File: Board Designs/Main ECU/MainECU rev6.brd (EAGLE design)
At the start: 120.6 x 78.9 mm, 191 parts, among them J1 JUMPER, J2 JUMPER, J3 JUMPER, J4 JUMPER, J5 JUMPER, J6 JUMPER, Q1 P-CHANNEL_MOSFET_DMP3099L-7, Q12 P-CHANNEL_MOSFET_DMP3099L-7, X1 CONNECTOR-37, X2 CONNECTOR-4AUTOSPORT, X3 CONNECTOR-4NANO-FIT-VERTICAL-4, X4 CONNECTOR-4NANO-FIT-VERTICAL-4

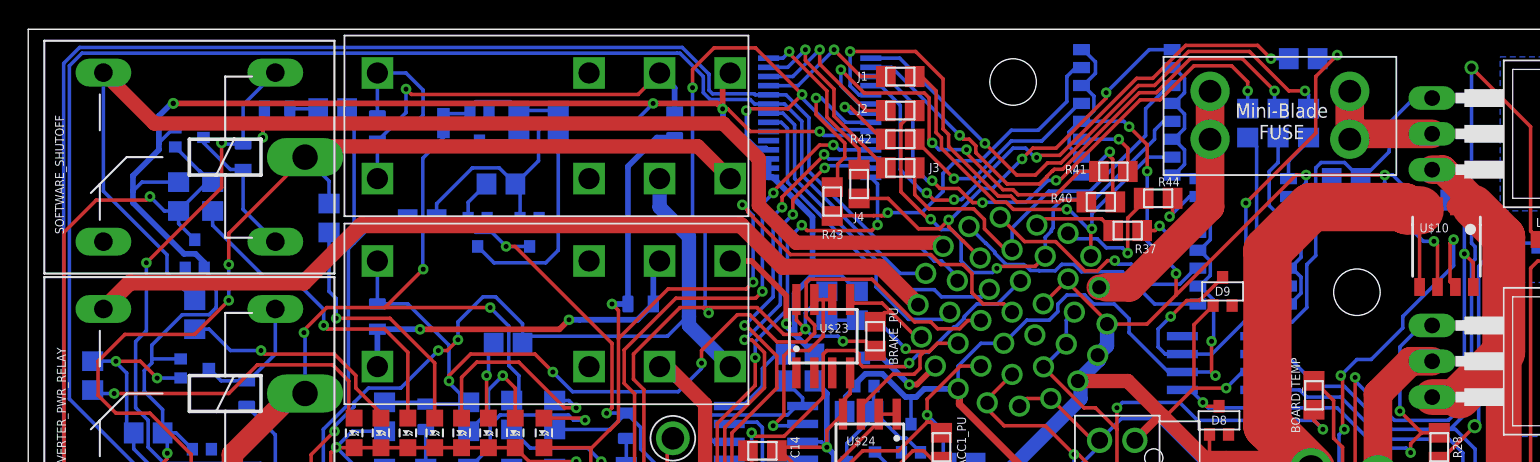
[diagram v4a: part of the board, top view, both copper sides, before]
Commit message: Main ECU rev6: Add optional diode to drop IMD relay coil voltage
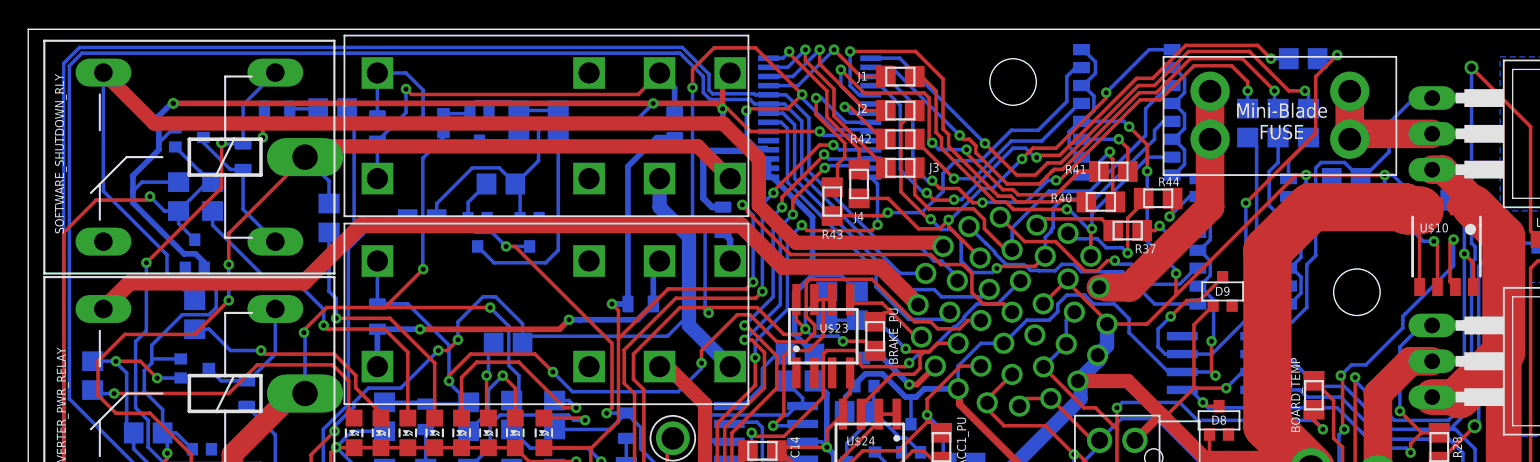
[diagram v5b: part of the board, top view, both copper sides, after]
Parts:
- added D23: TS4148 RYG, HyTechDevices:0805_D
- BMS_SHUTDOWN_RLY: value RT424009 -> RT424012
- renumbered IMD_SHUTDOWN to IMD_SHUTDOWN_RLY, IMD_SHUTDOWN1 to BMS_SHUTDOWN_RLY, SOFTWARE_SHUTOFF to SOFTWARE_SHUTDOWN_RLY
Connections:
- new net N$60: D23.A, IMD_SHUTDOWN_RLY.4
- net GND: now also D23.C; no longer IMD_SHUTDOWN_RLY.4
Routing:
- net N$60: track 0.00 -> 2.23 mm
- net GND: vias 36 -> 35
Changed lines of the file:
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@@
 <attribute name="VALUE" x="24.0538" y="58.547" size="0.3048" layer="28" font="vector" rot="MR90" align="top-center"/>
 </element>
-<element name="IMD_SHUTDOWN" library="HyTechDevices" package="RELAY_DPDT" value="RT424009" x="49.784" y="62.484" smashed="yes" rot="R180"/>
-<element name="IMD_SHUTDOWN1" library="HyTechDevices" package="RELAY_DPDT" value="RT424009" x="49.784" y="75.819" smashed="yes" rot="R180"/>
+<element name="IMD_SHUTDOWN_RLY" library="HyTechDevices" package="RELAY_DPDT" value="RT424009" x="49.784" y="62.484" smashed="yes" rot="R180"/>
+<element name="BMS_SHUTDOWN_RLY" library="HyTechDevices" package="RELAY_DPDT" value="RT424012" x="49.784" y="75.819" smashed="yes" rot="R180"/>
 <element name="LED1" library="HyTechDevices" package="LED-805" value="White" x="36.576" y="50.292" smashed="yes" rot="R180"/>
 <element name="LED10" library="HyTechDevices" package="LED-805" value="Red" x="35.56" y="32.639" smashed="yes" rot="R90"/>
@@
 <attribute name="VALUE" x="26.924" y="41.91" size="0.6096" layer="27" font="vector" ratio="20" rot="R180" align="top-center"/>
 </element>
-<element name="SOFTWARE_SHUTOFF" library="HyTechDevices" package="ZF112" value="G5LE" x="21.59" y="78.74" smashed="yes" rot="R180">
+<element name="SOFTWARE_SHUTDOWN_RLY" library="HyTechDevices" package="ZF112" value="G5LE" x="21.59" y="78.74" smashed="yes" rot="R180">
 <attribute name="NAME" x="2.54" y="64.389" size="0.635" layer="25" font="vector" rot="R90"/>
 </element>
@@
 <attribute name="VALUE" x="12.319" y="30.7848" size="0.3048" layer="28" rot="MR0" align="top-center"/>
 </element>
+<element name="D23" library="HyTechDevices" package="0805_D" value="TS4148 RYG" x="49.276" y="65.405" smashed="yes" rot="MR90">
+<attribute name="NAME" x="50.1269" y="65.024" size="0.635" layer="26" font="vector" rot="MR90" align="bottom-center"/>
+<attribute name="VALUE" x="48.5648" y="65.405" size="0.3048" layer="28" rot="MR90" align="top-center"/>
+</element>
 </elements>
 <signals>
@@
 <wire x1="51.21180625" y1="71.669" x2="56.134" y2="71.669" width="0.254" layer="1"/>
 <via x="56.134" y="71.669" extent="1-16" drill="0.35"/>
-<wire x1="51.693" y1="69.719" x2="49.276" y2="72.136" width="0.4064" layer="16"/>
+<wire x1="51.693" y1="69.719" x2="51.1175" y2="70.2945" width="0.4064" layer="16"/>
+<wire x1="51.1175" y1="70.2945" x2="49.276" y2="72.136" width="0.4064" layer="16"/>
 <wire x1="49.276" y1="72.136" x2="49.276" y2="73.24920625" width="0.4064" layer="16"/>
 <wire x1="56.134" y1="71.669" x2="56.4134" y2="71.3896" width="0.254" layer="16"/>
@@
 <wire x1="61.688" y1="32.512" x2="60.316" y2="32.512" width="0.254" layer="1"/>
 <wire x1="60.316" y1="32.512" x2="59.563" y2="31.759" width="0.254" layer="1"/>
-<contactref element="IMD_SHUTDOWN" pad="4"/>
-<contactref element="IMD_SHUTDOWN1" pad="4"/>
+<contactref element="BMS_SHUTDOWN_RLY" pad="4"/>
 <contactref element="Q2" pad="2"/>
 <contactref element="D18" pad="1"/>
-<wire x1="54.356" y1="57.277" x2="53.7619875" y2="57.8710125" width="0.4064" layer="16"/>
-<wire x1="53.7619875" y1="57.8710125" x2="53.7619875" y2="58.039" width="0.4064" layer="16"/>
-<via x="53.7619875" y="58.039" extent="1-16" drill="0.35"/>
-<wire x1="49.784" y1="62.484" x2="51.308" y2="62.484" width="0.4064" layer="1"/>
-<wire x1="53.7619875" y1="60.0300125" x2="53.7619875" y2="58.039" width="0.4064" layer="1"/>
-<wire x1="51.308" y1="62.484" x2="53.7619875" y2="60.0300125" width="0.4064" layer="1"/>
 <wire x1="48.86520625" y1="73.66" x2="44.323" y2="73.66" width="0.4064" layer="1"/>
 <wire x1="44.323" y1="73.66" x2="10.287" y2="73.66" width="0.4064" layer="1"/>
@@
 <wire x1="49.248403125" y1="73.276803125" x2="49.248403125" y2="75.283403125" width="0.4064" layer="1"/>
 <wire x1="49.248403125" y1="75.283403125" x2="49.784" y2="75.819" width="0.4064" layer="1"/>
+<contactref element="D23" pad="C"/>
+<wire x1="49.276" y1="66.305" x2="48.503" y2="66.305" width="0.4572" layer="16"/>
+<wire x1="48.503" y1="66.305" x2="47.879" y2="66.929" width="0.4572" layer="16"/>
+<wire x1="48.4505" y1="70.2945" x2="51.1175" y2="70.2945" width="0.4572" layer="16"/>
+<wire x1="47.879" y1="66.929" x2="47.879" y2="69.723" width="0.4572" layer="16"/>
+<wire x1="47.879" y1="69.723" x2="48.4505" y2="70.2945" width="0.4572" layer="16"/>
 </signal>
 <signal name="+12V">
@@
 <wire x1="7.62" y1="56.769" x2="8.382" y2="57.531" width="0.254" layer="16"/>
 <contactref element="D7" pad="C"/>
-<contactref element="SOFTWARE_SHUTOFF" pad="2"/>
+<contactref element="SOFTWARE_SHUTDOWN_RLY" pad="2"/>
 <wire x1="15.24" y1="70.7754" x2="15.24" y2="73.5584" width="0.254" layer="16"/>
 <wire x1="15.24" y1="73.5584" x2="17.526" y2="75.8444" width="0.254" layer="16"/>
@@
 </signal>
 <signal name="SHUTDOWN_C">
-<contactref element="IMD_SHUTDOWN1" pad="5"/>
-<contactref element="SOFTWARE_SHUTOFF" pad="P"/>
+<contactref element="BMS_SHUTDOWN_RLY" pad="5"/>
+<contactref element="SOFTWARE_SHUTDOWN_RLY" pad="P"/>
 <wire x1="49.784" y1="68.326" x2="47.498" y2="70.612" width="1.016" layer="1"/>
 <wire x1="20.3962" y1="70.612" x2="19.6342" y2="69.85" width="1.016" layer="1"/>
@@
 <wire x1="38.608" y1="53.213" x2="37.211" y2="54.61" width="0.254" layer="16"/>
 <contactref element="D6" pad="C"/>
-<contactref element="IMD_SHUTDOWN" pad="COIL+"/>
+<contactref element="IMD_SHUTDOWN_RLY" pad="COIL+"/>
 <wire x1="25.273" y1="52.46" x2="28.069" y2="52.46" width="0.254" layer="16"/>
 <wire x1="28.069" y1="52.46" x2="28.194" y2="52.335" width="0.254" layer="16"/>
@@
 </signal>
 <signal name="BMS_PWR_STEP">
-<contactref element="IMD_SHUTDOWN1" pad="3"/>
-<contactref element="IMD_SHUTDOWN1" pad="COIL-"/>
+<contactref element="BMS_SHUTDOWN_RLY" pad="3"/>
+<contactref element="BMS_SHUTDOWN_RLY" pad="COIL-"/>
 <contactref element="D5" pad="A"/>
 <contactref element="D16" pad="A"/>
@@
 </signal>
 <signal name="SHUTDOWN_B">
-<contactref element="IMD_SHUTDOWN1" pad="6"/>
-<contactref element="IMD_SHUTDOWN" pad="5"/>
+<contactref element="BMS_SHUTDOWN_RLY" pad="6"/>
+<contactref element="IMD_SHUTDOWN_RLY" pad="5"/>
 <wire x1="46.863" y1="64.2112" x2="44.7802" y2="66.294" width="1.016" layer="16"/>
 <wire x1="44.7802" y1="66.294" x2="44.7802" y2="68.326" width="1.016" layer="16"/>
@@
 </signal>
 <signal name="IMD_PWR_STEP">
-<contactref element="IMD_SHUTDOWN" pad="3"/>
-<contactref element="IMD_SHUTDOWN" pad="COIL-"/>
+<contactref element="IMD_SHUTDOWN_RLY" pad="3"/>
+<contactref element="IMD_SHUTDOWN_RLY" pad="COIL-"/>
 <contactref element="D6" pad="A"/>
 <contactref element="D15" pad="A"/>
@@
 </signal>
 <signal name="SHUTDOWN_A">
-<contactref element="IMD_SHUTDOWN" pad="6"/>
+<contactref element="IMD_SHUTDOWN_RLY" pad="6"/>
 <contactref element="5ASHUTDOWNFUSE" pad="R1"/>
 <contactref element="5ASHUTDOWNFUSE" pad="R2"/>
@@
 </signal>
 <signal name="SHUTDOWN_D">
-<contactref element="SOFTWARE_SHUTOFF" pad="S"/>
+<contactref element="SOFTWARE_SHUTDOWN_RLY" pad="S"/>
 <contactref element="R31" pad="1"/>
 <wire x1="8.9408" y1="72.2376" x2="5.334" y2="75.8444" width="1.016" layer="1"/>
@@
 <wire x1="93.345" y1="50.546" x2="92.964" y2="50.165" width="0.254" layer="16"/>
 <wire x1="92.964" y1="50.165" x2="92.964" y2="47.244" width="0.254" layer="16"/>
-<wire x1="94.234" y1="55.499" x2="93.091" y2="54.356" width="0.254" layer="16"/>
-<wire x1="94.234" y1="55.499" x2="95.25" y2="55.499" width="0.254" layer="16"/>
-<wire x1="97.4852" y1="57.7342" x2="95.25" y2="55.499" width="0.254" layer="16"/>
-<wire x1="97.4852" y1="57.7342" x2="97.4852" y2="58.547" width="0.254" layer="16"/>
+<wire x1="93.853" y1="55.118" x2="93.091" y2="54.356" width="0.254" layer="16"/>
+<wire x1="93.853" y1="55.118" x2="94.869" y2="55.118" width="0.254" layer="16"/>
+<wire x1="97.4852" y1="57.7342" x2="94.869" y2="55.118" width="0.254" layer="16"/>
+<wire x1="97.4852" y1="57.7342" x2="97.4852" y2="58.293" width="0.254" layer="16"/>
+<wire x1="97.4852" y1="58.293" x2="97.4852" y2="58.547" width="0.254" layer="16"/>
 <wire x1="98.298" y1="35.56" x2="99.314" y2="35.56" width="0.254" layer="16"/>
 <wire x1="100.956" y1="33.918" x2="101.727" y2="33.918" width="0.254" layer="16"/>
 <wire x1="99.314" y1="35.56" x2="100.956" y2="33.918" width="0.254" layer="16"/>
-<wire x1="97.4852" y1="58.547" x2="101.092" y2="62.1538" width="0.254" layer="16"/>
+<wire x1="97.4852" y1="58.547" x2="97.6376" y2="58.6994" width="0.254" layer="16"/>
+<wire x1="97.6376" y1="58.6994" x2="101.092" y2="62.1538" width="0.254" layer="16"/>
 <wire x1="101.092" y1="62.1538" x2="101.092" y2="64.008" width="0.254" layer="16"/>
 </signal>
@@
 </signal>
 <signal name="N$27">
-<contactref element="SOFTWARE_SHUTOFF" pad="1"/>
+<contactref element="SOFTWARE_SHUTDOWN_RLY" pad="1"/>
 <contactref element="D7" pad="A"/>
 <wire x1="15.24" y1="68.9754" x2="15.24" y2="66.1416" width="0.254" layer="16"/>
@@
 </signal>
 <signal name="BMS_OK_SW">
-<contactref element="IMD_SHUTDOWN1" pad="COIL+"/>
+<contactref element="BMS_SHUTDOWN_RLY" pad="COIL+"/>
 <contactref element="D5" pad="C"/>
 <wire x1="24.765" y1="75.819" x2="24.765" y2="72.782" width="0.254" layer="16"/>
@@
 <wire x1="11.41" y1="31.505" x2="11.419" y2="31.496" width="0.254" layer="16"/>
 </signal>
+<signal name="N$60">
+<contactref element="IMD_SHUTDOWN_RLY" pad="4"/>
+<contactref element="D23" pad="A"/>
+<wire x1="49.784" y1="62.484" x2="49.784" y2="63.997" width="0.4572" layer="16"/>
+<wire x1="49.784" y1="63.997" x2="49.276" y2="64.505" width="0.4572" layer="16"/>
+</signal>
 </signals>

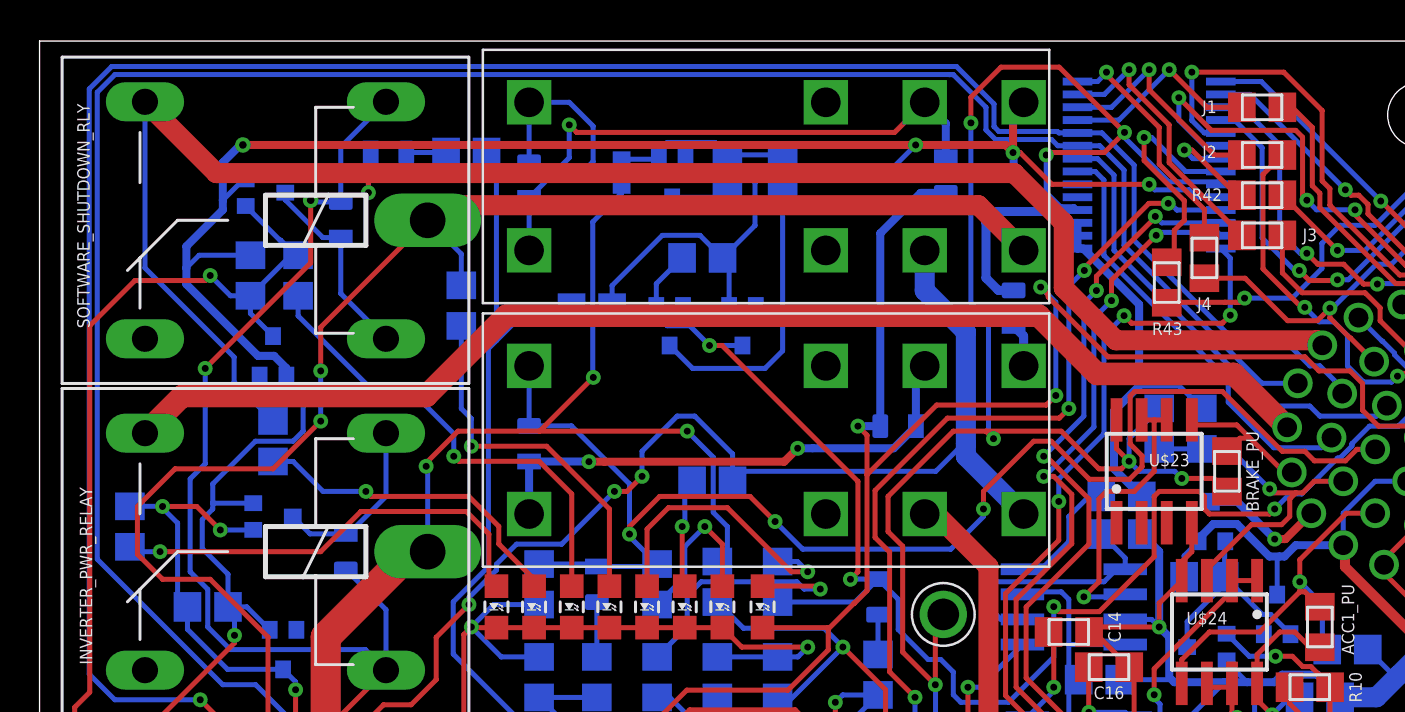
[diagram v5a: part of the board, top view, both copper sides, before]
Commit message: Main ECU rev5/6: Add jumpers for DASH 11/12 so we can safely monitor 12V signals on those channels
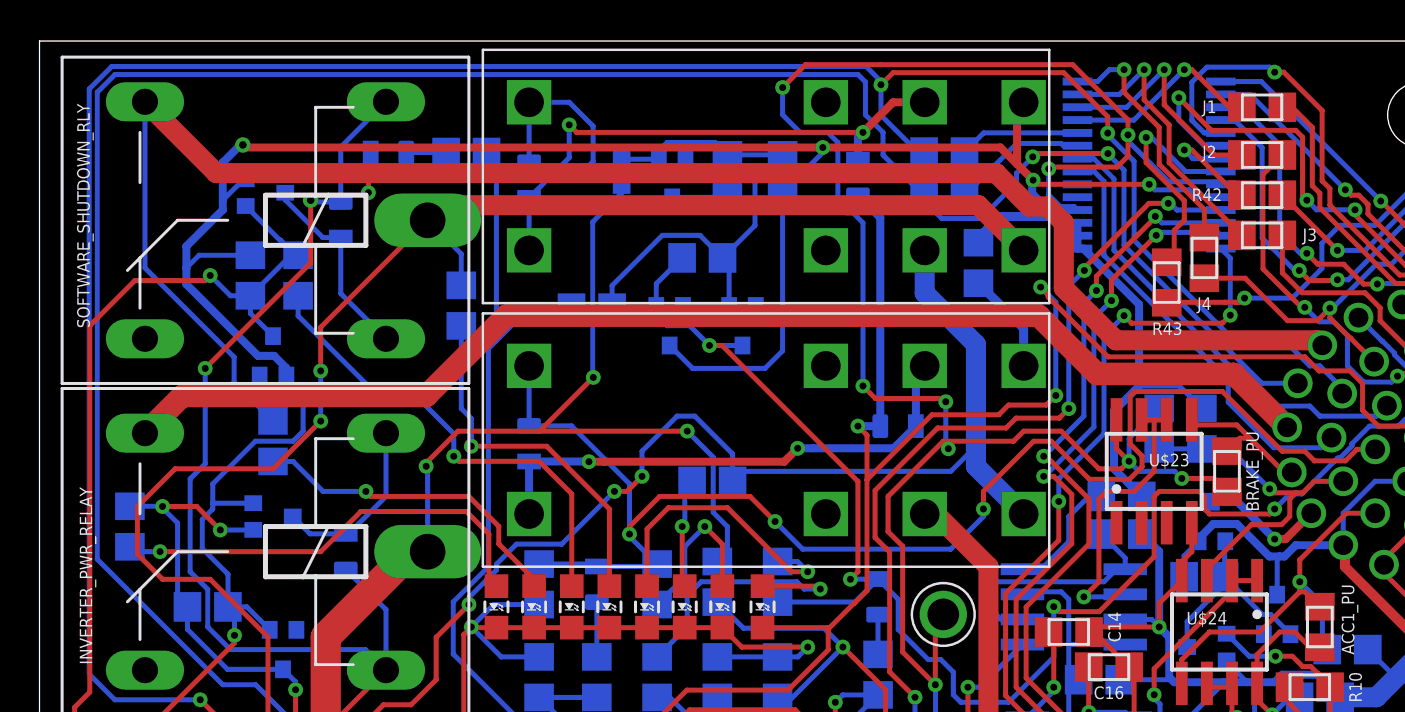
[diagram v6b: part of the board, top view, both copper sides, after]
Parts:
- removed D23: TS4148 RYG, HyTechDevices:0805_D
- added J7, J8: JUMPER, HyTechDevices:0805
- added R63: (no value), HyTechDevices:0805
- moved D16 4.45 mm to (41.4, 72.0)
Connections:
- net DASH_CTRL1 renamed DASH_1_SWITCH
- net DASH_CTRL10 renamed DASH_10_IO
- net DASH_CTRL11_READ renamed DASH11_READ
- net DASH_CTRL12_READ renamed DASH12_READ
- net DASH_CTRL2 renamed DASH_2_SWITCH
- net DASH_CTRL3 renamed DASH_3_SWITCH
- net DASH_CTRL4 renamed DASH_4_SWITCH
- net DASH_CTRL5_IN renamed DASH_5_READ
- net DASH_CTRL5_OUT renamed DASH_5_SWITCH
- net DASH_CTRL6_IN renamed DASH_6_READ
- net DASH_CTRL6_OUT renamed DASH_6_SWITCH
- net DASH_CTRL7_IN renamed DASH_7_READ
- net DASH_CTRL7_OUT renamed DASH_7_SWITCH
- net DASH_CTRL8_IN renamed DASH_8_READ
- net DASH_CTRL8_OUT renamed DASH_8_SWITCH
- net DASH_CTRL9 renamed DASH_9_IO
- net DASH_IO1 renamed DASH_1_OUT
- net DASH_IO2 renamed DASH_2_OUT
- net DASH_IO3 renamed DASH_3_OUT
- net DASH_IO4 renamed DASH_4_OUT
- net DASH_IO5 renamed DASH_5_IO
- net DASH_IO6 renamed DASH_6_IO
- net DASH_IO7 renamed DASH_7_IO
- net DASH_IO8 renamed DASH_8_IO
- removed net DASH_CTRL11: D19.A, U$17.23, X1.P$6
- removed net DASH_CTRL12: D20.A, U$17.24, X1.P$22
- new net DASH_11_IO: D19.A, J7.1, X1.P$6
- new net DASH_11_OPT: J7.2, U$17.23
- new net DASH_12_IO: D20.A, J8.1, X1.P$22
- new net DASH_12_OPT: J8.2, U$17.24
- net GND: now also R63.2; no longer D23.C
- net N$60: now also R63.1; no longer D23.A
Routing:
- net DASH_12_IO: track 0.00 -> 122.8 mm, vias 0 -> 4
- net DASH_CTRL12: track 117.7 -> 0.00 mm, vias 2 -> 0
- net DASH_11_IO: track 0.00 -> 112.1 mm, vias 0 -> 2
- net DASH_CTRL11: track 108.0 -> 0.00 mm
- net +5V: track 345.2 -> 362.2 mm, vias 13 -> 15
- net GND: track 927.5 -> 918.2 mm
- net DASH_11_OPT: track 0.00 -> 6.86 mm
- net DASH_12_OPT: track 0.00 -> 6.11 mm
- net N$60: track 2.23 -> 5.13 mm
- net BMS_PWR_STEP: track 29.2 -> 27.5 mm, vias 1 -> 2
- net LATCH_EXT_BUTTON: track 92.7 -> 91.1 mm
- net DASH_8_READ: track 12.1 -> 12.8 mm
